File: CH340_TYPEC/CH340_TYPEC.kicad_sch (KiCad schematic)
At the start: 14 parts, among them J1 UART_OUT, P1 USB_C_Plug_USB2.0, U1 CH340G, Y1 16MHz

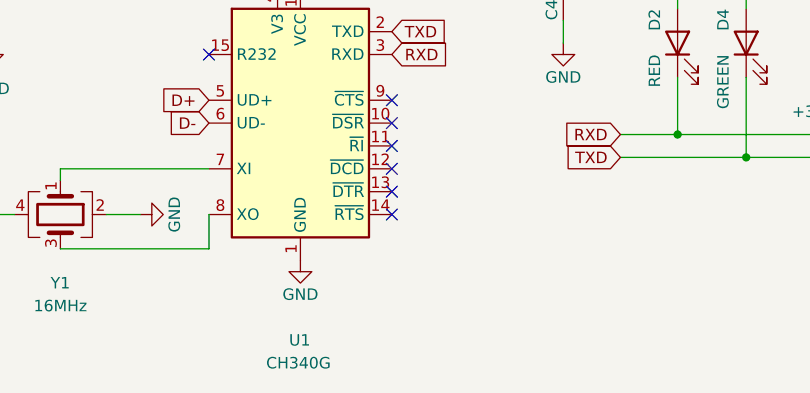
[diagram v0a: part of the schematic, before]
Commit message: Update CH340_TYPEC.kicad_sch
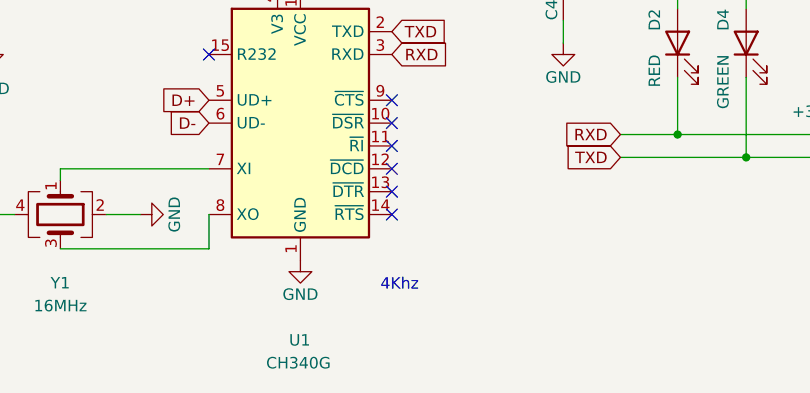
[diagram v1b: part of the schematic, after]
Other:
- note added: "4Khz"
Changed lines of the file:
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@@
     (stroke (width 0) (type default) (color 0 0 0 0))
+  )
+  (text "4Khz\n" (at 171.45 116.586 0)
+    (effects (font (size 1.27 1.27)) (justify left bottom))
   )
   (global_label "D+" (shape input) (at 152.4 95.25 180) (fields_autoplaced)
